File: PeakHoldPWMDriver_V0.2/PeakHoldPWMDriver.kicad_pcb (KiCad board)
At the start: 2 copper layers, 100.1 x 50 mm, 81 parts, among them J1 Screw_Terminal_01x06, J2 Screw_Terminal_01x08, J3 Mounting 3mm, J4 Mounting 3mm, J5 Mounting 3mm, J6 Mounting 3mm, Q1 AO3400, Q10 AO3400, Q11 AO3422, Q12 AO3422, Q13 AO3401A, Q14 BSP78, Q15 AO3401A, Q16 BSP78, Q2 AO3400, Q3 AO3422, Q4 AO3422, Q5 AO3401A, Q6 AO3401A, Q7 BSP78, Q8 BSP78, Q9 AO3400, U1 74LS32, U2 LM2901, U3 74LS74, U4 LTC6992, U5 74LS74, U6 LM78M05_TO220, U7 74LS08, U8 74LS08

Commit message: Routing board V0.2
Work done on new PCB
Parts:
- removed the D6 at (126.6, 101.9)
- removed the D7 at (149.6, 101.9)
- removed J3, J4, J5, J6: Mounting 3mm, MountingHole:MountingHole_3.2mm_M3_DIN965_Pad
- removed the R6 at (130.4, 101.9)
- removed the U7 at (166.0, 104.4)
- added C1: SVPF 1,0M 16, Capacitor_SMD:CP_Elec_10x12.5, F.Cu at (149.9, 101.6)
- added C10: 220nf, Capacitor_SMD:C_0603_1608Metric_Pad1.05x0.95mm_HandSolder, F.Cu at (141.1, 71.4)
- added C2: SVPF 1,0M 16, Capacitor_SMD:CP_Elec_10x12.5, F.Cu at (149.9, 79.8)
- added C3: SVPF 1,0M 16, Capacitor_SMD:CP_Elec_10x12.5, F.Cu at (149.9, 90.7)
- added H1: MountingHole_Pad, MountingHole:MountingHole_2.5mm_Pad, F.Cu at (125.7, 69.8)
- added H2: MountingHole_Pad, MountingHole:MountingHole_2.5mm_Pad, F.Cu at (125.7, 111.8)
- added H3: MountingHole_Pad, MountingHole:MountingHole_2.5mm_Pad, F.Cu at (201.4, 69.8)
- added H4: MountingHole_Pad, MountingHole:MountingHole_2.5mm_Pad, F.Cu at (201.4, 111.8)
- added R8: 8K2, Resistor_SMD:R_0603_1608Metric_Pad1.05x0.95mm_HandSolder, F.Cu at (141.1, 68.3)
- added TP1: PeakTP, TestPoint:TestPoint_Pad_1.0x1.0mm, F.Cu at (207.3, 68.3)
- added TP2: HoldTP, TestPoint:TestPoint_Pad_1.0x1.0mm, F.Cu at (142.0, 73.7)
- added U8: 74LS08, Package_SO:SO-14_5.3x10.2mm_P1.27mm, F.Cu at (161.0, 109.2)
- D1, D4: value LL4148 -> BAV103
- D3: value 40V-1A -> 1N4007
- D6: renamed from D8; value SS310 -> 1N4007
- D7: renamed from D9; value SS310 -> 1N4007
- D8: renamed from D10; value SS310 -> 1N4007
- D9: renamed from D11; value SS310 -> 1N4007
- J1: footprint Connector_Phoenix_MSTB:PhoenixContact_MSTBV_2,5_6-GF-5,08_1x06_P5.08mm_Vertical_ThreadedFlange -> Connector_Phoenix_MSTB:PhoenixContact_MSTBA_2,5_6-G-5,08_1x06_P5.08mm_Horizontal
- J2: footprint Connector_Phoenix_MSTB:PhoenixContact_MSTBV_2,5_8-GF-5,08_1x08_P5.08mm_Vertical_ThreadedFlange -> Connector_Phoenix_MSTB:PhoenixContact_MSTBA_2,5_8-G-5,08_1x08_P5.08mm_Horizontal
- Q11, Q12, Q3, Q4: value AO3422 -> 2N7002
- Q13, Q15, Q5, Q6: value AO3401A -> TSM2309
- U6: footprint Package_TO_SOT_THT:TO-220-3_Vertical -> Package_TO_SOT_SMD:SOT-223-3_TabPin2
- moved D4 43.2 mm to (191.8, 73.4)
- moved R6 40.6 mm to (196.2, 73.2)
- moved RV2 30.4 mm to (193.8, 69.3)
- moved C5 28.2 mm to (126.0, 105.2), turned to 180 degrees
- moved J1 27.2 mm to (115.8, 76.7), turned to 270 degrees
- moved C8 23.8 mm to (131.6, 105.2), turned to 0 degrees
- moved U3 22.5 mm to (171.9, 109.2), turned to 0 degrees
- moved C9 22.4 mm to (136.3, 105.2), turned to 0 degrees
- moved C7 21.0 mm to (136.3, 107.7), turned to 0 degrees
- moved R1 18.2 mm to (114.9, 112.8), turned to 45 degrees
- moved U5 18.1 mm to (171.9, 72.9), turned to 0 degrees
- moved F2 16.9 mm to (121.7, 99.6)
- moved RV1 16.7 mm to (117.9, 69.6)
- moved D3 12.5 mm to (127.0, 99.6), turned to 90 degrees
- moved R18 12.5 mm to (174.5, 101.9), turned to 0 degrees
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- renumbered C1 to C5, C2 to C6, C3 to C7, C4 to C8, C5 to C9, R7 to R6, R8 to R7, U8 to U7
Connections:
- C5 pad 2: Net-(C1-Pad2) -> Net-(C5-Pad2)
- C7 pad 2: Net-(C1-Pad2) -> Net-(C5-Pad2)
- D3 pad 1: Net-(D3-Pad1) -> Net-(C5-Pad2)
- D3 pad 2: Net-(C1-Pad2) -> Net-(D3-Pad2)
- F2 pad 2: Net-(D3-Pad1) -> Net-(D3-Pad2)
- J1 pad 1: VBAT_IN -> INJ4
- J1 pad 2: PWR_GND -> INJ3
- J1 pad 3: INJ1 -> INJ2
- J1 pad 4: INJ2 -> INJ1
- J1 pad 5: INJ3 -> PWR_GND
- J1 pad 6: INJ4 -> VBAT_IN
- U2 pad 10: VREF -> Net-(Q16-Pad3)
- U2 pad 11: Net-(Q8-Pad3) -> VREF
- U2 pad 13: Net-(R19-Pad2) -> Net-(R31-Pad2)
- U2 pad 14: Net-(R31-Pad2) -> Net-(R19-Pad2)
- U2 pad 4: VREF -> Net-(Q7-Pad3)
- U2 pad 5: Net-(Q7-Pad3) -> VREF
- U2 pad 6: VREF -> Net-(Q14-Pad3)
- U2 pad 7: Net-(Q14-Pad3) -> VREF
- U2 pad 8: VREF -> Net-(Q8-Pad3)
- U2 pad 9: Net-(Q16-Pad3) -> VREF
- U6 pad 1: Net-(C1-Pad2) -> Net-(C5-Pad2)
- U7 pad 10: inv_INJ4 -> inv_INJ3
- U7 pad 11: Net-(U1-Pad13) -> Net-(U1-Pad10)
- U7 pad 12: Net-(U5-Pad8) -> Net-(U5-Pad6)
- U7 pad 13: inv_INJ4 -> inv_INJ3
- U7 pad 2: inv_INJ3 -> inv_INJ1
- U7 pad 3: Net-(U1-Pad9) -> Net-(U1-Pad1)
- U7 pad 4: Net-(U5-Pad6) -> Net-(U5-Pad8)
- U7 pad 5: inv_INJ3 -> inv_INJ4
- U7 pad 6: Net-(U1-Pad10) -> Net-(U1-Pad13)
- U7 pad 8: Net-(U1-Pad12) -> Net-(U1-Pad9)
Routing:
- net PWR_GND: track 509.7 -> 63.6 mm, vias 56 -> 0
- net 5V: track 253.7 -> 0.00 mm, vias 18 -> 0
- net PWM: track 84.8 -> 0.00 mm, vias 6 -> 0
- net inv_INJ2: track 70.8 -> 0.00 mm, vias 2 -> 0
- net Net-(Q5-Pad1): track 64.8 -> 0.00 mm, vias 3 -> 0
- net inv_INJ3: track 64.8 -> 0.00 mm, vias 3 -> 0
- net inv_INJ4: track 63.4 -> 0.00 mm, vias 3 -> 0
- net Net-(Q13-Pad1): track 56.4 -> 0.00 mm, vias 2 -> 0
- net Net-(Q15-Pad1): track 47.6 -> 0.00 mm, vias 2 -> 0
- net inv_INJ1: track 46.0 -> 0.00 mm, vias 3 -> 0
- net Net-(Q7-Pad1): track 44.0 -> 0.00 mm, vias 2 -> 0
- net Net-(Q6-Pad1): track 38.6 -> 0.00 mm, vias 2 -> 0
- net Net-(Q16-Pad1): track 36.3 -> 0.00 mm, vias 2 -> 0
- net Net-(C1-Pad2): track 32.2 -> 0.00 mm
- net Net-(U5-Pad8): track 31.6 -> 0.00 mm
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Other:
- board text removed: "13.8V"
- board text removed: "5V"

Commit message: routed V0.2
New board fully routed
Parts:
- D6, D7, D8, D9: value 1N4007 -> SS33
- moved RV1 29.3 mm to (147.2, 70.1), turned to 180 degrees
- moved D1 24.2 mm to (154.2, 70.1)
- moved R2 20.7 mm to (151.4, 70.2), turned to 270 degrees
- moved U1 10.9 mm to (162.3, 91.4)
- moved R3 10.7 mm to (120.1, 69.2), turned to 90 degrees
- moved U2 10.3 mm to (173.6, 91.4)
- moved R28 8.07 mm to (184.3, 94.7), turned to 180 degrees
- moved R17 7.68 mm to (184.3, 88.1), turned to 180 degrees
- moved R24 7.11 mm to (130.9, 77.7)
- moved R16 6.62 mm to (191.0, 99.9)
- moved U4 5.78 mm to (131.1, 70.9), turned to 90 degrees
- moved R18 5.59 mm to (168.9, 101.9), turned to 180 degrees
- moved R29 5.45 mm to (174.9, 101.9), turned to 0 degrees
- moved R11 5.33 mm to (131.0, 82.5)
- moved R22 3.56 mm to (131.0, 87.4)
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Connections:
- U2 pad 10: Net-(Q16-Pad3) -> Net-(Q8-Pad3)
- U2 pad 13: Net-(R31-Pad2) -> Net-(R19-Pad2)
- U2 pad 14: Net-(R19-Pad2) -> Net-(R31-Pad2)
- U2 pad 8: Net-(Q8-Pad3) -> Net-(Q16-Pad3)
- U7 pad 2: inv_INJ1 -> inv_INJ4
- U7 pad 3: Net-(U1-Pad1) -> Net-(U1-Pad12)
- U8 pad 10: inv_INJ4 -> inv_INJ1
- U8 pad 8: Net-(U1-Pad12) -> Net-(U1-Pad1)
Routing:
- net PWR_GND: track 63.6 -> 458.5 mm, vias 0 -> 62
- net 5V: track 0.00 -> 310.1 mm, vias 0 -> 21
- net PWM: track 0.00 -> 115.9 mm, vias 0 -> 7
- net inv_INJ2: track 0.00 -> 78.9 mm, vias 0 -> 2
- net inv_INJ1: track 0.00 -> 72.8 mm, vias 0 -> 2
- net inv_INJ3: track 0.00 -> 69.4 mm, vias 0 -> 2
- net inv_INJ4: track 0.00 -> 68.7 mm
- net Net-(Q5-Pad1): track 0.00 -> 65.2 mm, vias 0 -> 2
- net Net-(Q13-Pad1): track 0.00 -> 59.8 mm, vias 0 -> 2
- net Net-(Q15-Pad1): track 0.00 -> 58.8 mm, vias 0 -> 2
- net VREF: track 18.6 -> 76.6 mm, vias 0 -> 3
- net Net-(Q16-Pad1): track 0.00 -> 54.5 mm, vias 0 -> 4
- net Net-(Q7-Pad1): track 0.00 -> 52.5 mm, vias 0 -> 4
- net Net-(Q6-Pad1): track 0.00 -> 45.9 mm, vias 0 -> 2
- net Net-(Q14-Pad1): track 0.00 -> 42.2 mm
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- added copper zone on F.Cu, net INJ1-OUT
- added copper zone on F.Cu, net INJ2-OUT
- added copper zone on F.Cu, net INJ3-OUT
- added copper zone on F.Cu, net INJ4-OUT
- added copper zone on B.Cu, net inv_INJ1

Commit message: Cleanup of board
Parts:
- C1, C2, C3: value SVPF 1,0M 16 -> 1mF
- D2: value SS310 -> BAV103
- D6, D7, D8, D9: value SS33 -> SS36
- R14, R15, R2, R26, R27, R6: value 470 -> 470R
- R5: value 180 -> 180R
- R8: value 8K2 -> 10k
- U6: value LM78M05_TO220 -> LM78M05
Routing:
- net PWR_GND: track 458.5 -> 446.9 mm, vias 62 -> 99
- net Net-(Q14-Pad3): track 36.4 -> 39.6 mm
- net Net-(Q14-Pad1): track 42.2 -> 44.3 mm
- net Net-(Q8-Pad1): track 42.2 -> 43.3 mm
- net VBAT: vias 13 -> 14
- net INJ1-OUT: vias 0 -> 5
- net INJ4-OUT: vias 0 -> 3
- net INJ3-OUT: vias 0 -> 4
- net INJ2-OUT: vias 0 -> 3
- added copper zone on B.Cu, net INJ1-OUT
- added copper zone on B.Cu, net INJ2-OUT
- added copper zone on B.Cu, net INJ3-OUT
- added copper zone on B.Cu, net INJ4-OUT
- removed copper zone on B.Cu, net inv_INJ1
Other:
- board text added: "PWM Peak&Hold Injector driver"
- board text added: "by Tjeerd V0.2"
- board text removed: "PWM Peak&Hold Injector driver 4Cyl. by Tjeerd"

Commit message: further clean-up
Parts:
- moved R13 0.28 mm to (141.7, 83.3)
- moved R25 0.28 mm to (141.7, 78.5)
- moved RV1 0.20 mm to (147.3, 70.3)
- moved C10 0.14 mm to (141.0, 71.4)
- moved C6 0.14 mm to (137.7, 74.7)
- moved R10 0.14 mm to (130.8, 92.5)
- moved R11 0.14 mm to (130.8, 82.5)
- moved R22 0.14 mm to (130.8, 87.4)
- moved R8 0.14 mm to (141.0, 68.3)
- moved D5 0.11 mm to (121.2, 94.2)
- moved R12 0.11 mm to (141.7, 93.0)
- moved R14 0.11 mm to (179.1, 113.8)
- moved R19 0.11 mm to (169.2, 80.5)
- moved R2 0.11 mm to (151.4, 70.4)
- moved R24 0.11 mm to (130.8, 77.7)
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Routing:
- net VBAT: vias 14 -> 13

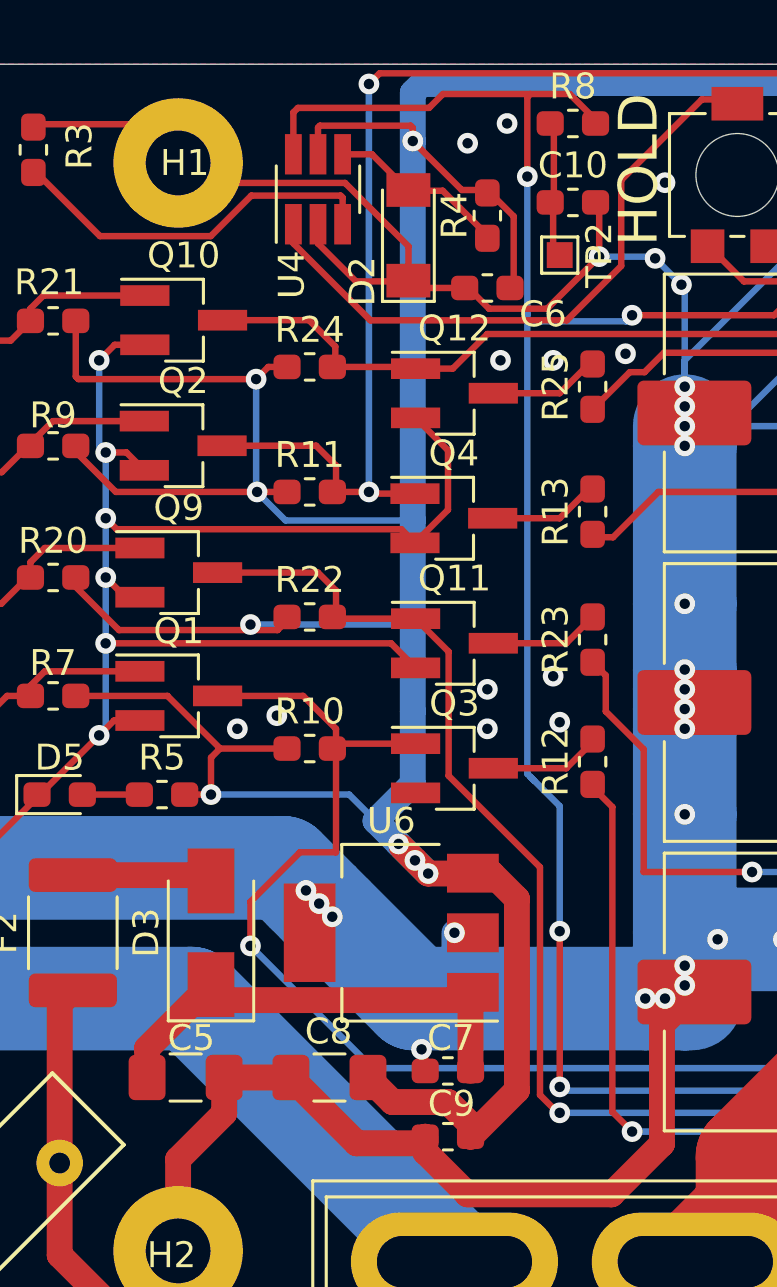
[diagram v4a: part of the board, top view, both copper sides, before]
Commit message: renumber all parts
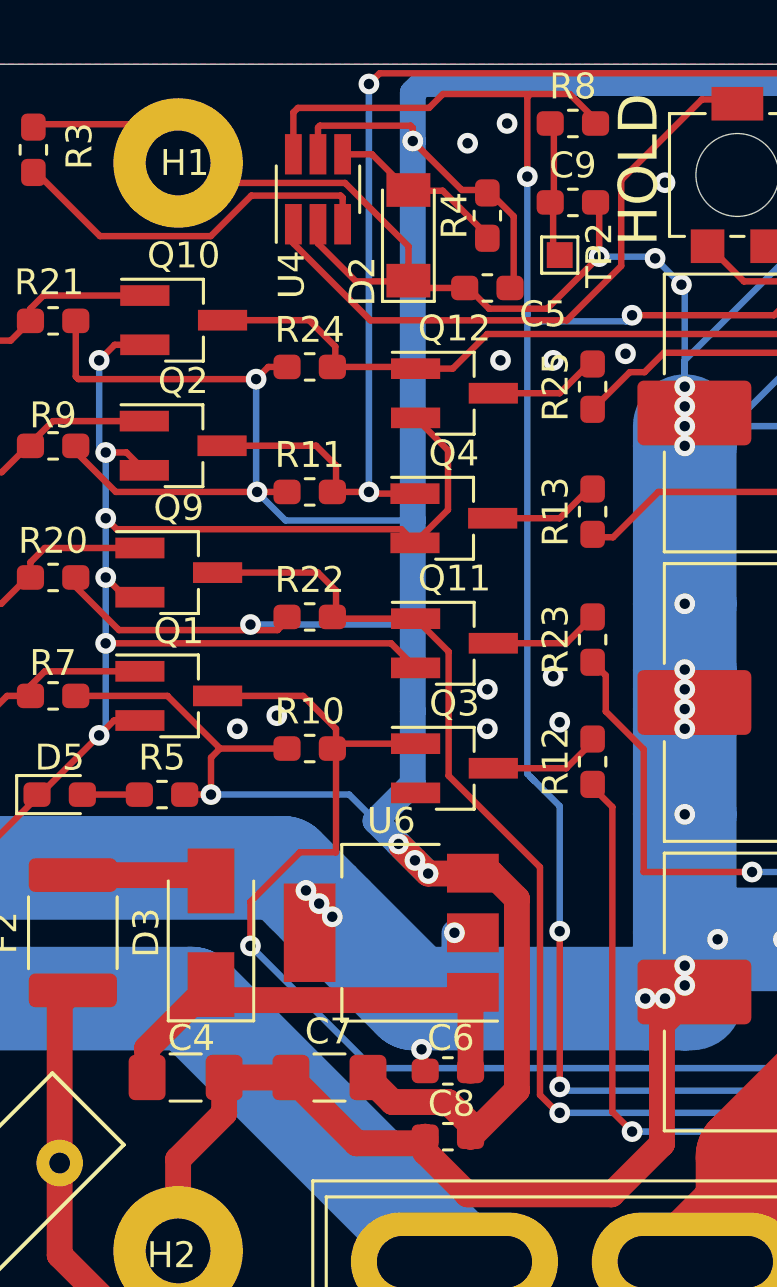
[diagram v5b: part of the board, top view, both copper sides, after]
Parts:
- renumbered C5 to C4, C6 to C5, C7 to C6, C8 to C7, C9 to C8, C10 to C9
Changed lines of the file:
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@@
   (net 62 "Net-(U5-Pad9)")
   (net 63 "Net-(U5-Pad5)")
-  (net 64 "Net-(C5-Pad2)")
-  (net 65 "Net-(C10-Pad1)")
-  (net 66 "Net-(D3-Pad2)")
-  (net 67 "Net-(D7-Pad2)")
+  (net 64 "Net-(D3-Pad2)")
+  (net 65 "Net-(D7-Pad2)")
+  (net 66 "Net-(C4-Pad2)")
+  (net 67 "Net-(C9-Pad1)")
   (net_class Default "This is the default net class."
     (clearance 0.2)
@@
     (add_net INJ4)
     (add_net INJ4-OUT)
-    (add_net "Net-(C10-Pad1)")
-    (add_net "Net-(C5-Pad2)")
+    (add_net "Net-(C4-Pad2)")
+    (add_net "Net-(C9-Pad1)")
     (add_net "Net-(D1-Pad2)")
     (add_net "Net-(D2-Pad2)")
@@
     )
     (pad 2 smd rect (at 2 0 90) (size 2.5 1.8) (layers F.Cu F.Paste F.Mask)
-      (net 66 "Net-(D3-Pad2)"))
+      (net 64 "Net-(D3-Pad2)"))
     (pad 1 smd rect (at -2 0 90) (size 2.5 1.8) (layers F.Cu F.Paste F.Mask)
-      (net 64 "Net-(C5-Pad2)"))
+      (net 66 "Net-(C4-Pad2)"))
     (model ${KISYS3DMOD}/Diode_SMD.3dshapes/D_SMA.wrl
       (at (xyz 0 0 0))
@@
     )
     (pad 2 smd rect (at 2 0 180) (size 2.5 1.8) (layers F.Cu F.Paste F.Mask)
-      (net 67 "Net-(D7-Pad2)"))
+      (net 65 "Net-(D7-Pad2)"))
     (pad 1 smd rect (at -2 0 180) (size 2.5 1.8) (layers F.Cu F.Paste F.Mask)
       (net 2 VBAT))
@@
     )
     (pad 1 smd rect (at -3.15 -2.3 180) (size 2 1.5) (layers F.Cu F.Paste F.Mask)
-      (net 64 "Net-(C5-Pad2)"))
+      (net 66 "Net-(C4-Pad2)"))
     (pad 3 smd rect (at -3.15 2.3 180) (size 2 1.5) (layers F.Cu F.Paste F.Mask)
       (net 1 5V))
@@
     )
     (pad 1 smd rect (at 0 0 90) (size 1 1) (layers F.Cu F.Mask)
-      (net 65 "Net-(C10-Pad1)"))
+      (net 67 "Net-(C9-Pad1)"))
   )
   (module TestPoint:TestPoint_Pad_1.0x1.0mm (layer F.Cu)
@@
       (net 14 PWM))
     (pad 1 smd roundrect (at -0.875 0) (size 1.05 0.95) (layers F.Cu F.Paste F.Mask) (roundrect_rratio 0.25)
-      (net 65 "Net-(C10-Pad1)"))
+      (net 67 "Net-(C9-Pad1)"))
     (model ${KISYS3DMOD}/Resistor_SMD.3dshapes/R_0603_1608Metric.wrl
       (at (xyz 0 0 0))
@@
     (tags "capacitor handsolder")
     (attr smd)
-    (fp_text reference C10 (at 0 -1.43) (layer F.SilkS)
+    (fp_text reference C9 (at 0 -1.43) (layer F.SilkS)
       (effects (font (size 1 1) (thickness 0.15)))
     )
@@
       (net 17 PWR_GND))
     (pad 1 smd roundrect (at -0.875 0) (size 1.05 0.95) (layers F.Cu F.Paste F.Mask) (roundrect_rratio 0.25)
-      (net 65 "Net-(C10-Pad1)"))
+      (net 67 "Net-(C9-Pad1)"))
     (model ${KISYS3DMOD}/Capacitor_SMD.3dshapes/C_0603_1608Metric.wrl
       (at (xyz 0 0 0))
@@
     )
     (pad 3 smd rect (at 1.5 0 180) (size 1.9 0.8) (layers F.Cu F.Paste F.Mask)
-      (net 67 "Net-(D7-Pad2)"))
+      (net 65 "Net-(D7-Pad2)"))
     (pad 2 smd rect (at -1.5 0.95 180) (size 1.9 0.8) (layers F.Cu F.Paste F.Mask)
       (net 5 INJ3-OUT))
@@
     )
     (pad 2 smd roundrect (at 2.225 0 90) (size 1.3 3.4) (layers F.Cu F.Paste F.Mask) (roundrect_rratio 0.192308)
-      (net 66 "Net-(D3-Pad2)"))
+      (net 64 "Net-(D3-Pad2)"))
     (pad 1 smd roundrect (at -2.225 0 90) (size 1.3 3.4) (layers F.Cu F.Paste F.Mask) (roundrect_rratio 0.192308)
       (net 2 VBAT))
@@
     (tags "capacitor handsolder")
     (attr smd)
-    (fp_text reference C8 (at -0.0365 -1.778) (layer F.SilkS)
+    (fp_text reference C7 (at -0.0365 -1.778) (layer F.SilkS)
       (effects (font (size 1 1) (thickness 0.15)))
     )
@@
     (tags "capacitor handsolder")
     (attr smd)
-    (fp_text reference C5 (at -0.2175 1.524) (layer F.SilkS)
+    (fp_text reference C4 (at -0.2175 1.524) (layer F.SilkS)
       (effects (font (size 1 1) (thickness 0.15)))
     )
@@
     )
     (pad 2 smd roundrect (at 1.4875 0 180) (size 1.425 1.75) (layers F.Cu F.Paste F.Mask) (roundrect_rratio 0.175439)
-      (net 64 "Net-(C5-Pad2)"))
+      (net 66 "Net-(C4-Pad2)"))
     (pad 1 smd roundrect (at -1.4875 0 180) (size 1.425 1.75) (layers F.Cu F.Paste F.Mask) (roundrect_rratio 0.175439)
       (net 17 PWR_GND))
@@
     (tags "capacitor handsolder")
     (attr smd)
-    (fp_text reference C6 (at -2.145 -1.016) (layer F.SilkS)
+    (fp_text reference C5 (at -2.145 -1.016) (layer F.SilkS)
       (effects (font (size 1 1) (thickness 0.15)))
     )
@@
     (tags "capacitor handsolder")
     (attr smd)
-    (fp_text reference C9 (at 0.141 -1.27) (layer F.SilkS)
+    (fp_text reference C8 (at 0.141 -1.27) (layer F.SilkS)
       (effects (font (size 1 1) (thickness 0.15)))
     )
@@
     (tags "capacitor handsolder")
     (attr smd)
-    (fp_text reference C7 (at 0.113 -1.27) (layer F.SilkS)
+    (fp_text reference C6 (at 0.113 -1.27) (layer F.SilkS)
       (effects (font (size 1 1) (thickness 0.15)))
     )
@@
     )
     (pad 2 smd roundrect (at 0.875 0) (size 1.05 0.95) (layers F.Cu F.Paste F.Mask) (roundrect_rratio 0.25)
-      (net 64 "Net-(C5-Pad2)"))
+      (net 66 "Net-(C4-Pad2)"))
     (pad 1 smd roundrect (at -0.875 0) (size 1.05 0.95) (layers F.Cu F.Paste F.Mask) (roundrect_rratio 0.25)
       (net 17 PWR_GND))
@@
   (segment (start 166.878 112.014) (end 168.335 112.014) (width 0.25) (layer F.Cu) (net 60) (status 20))
   (segment (start 166.624 111.76) (end 166.878 112.014) (width 0.25) (layer F.Cu) (net 60))
-  (segment (start 124.533 104.035) (end 127 101.568) (width 1) (layer F.Cu) (net 64) (status 20))
-  (segment (start 124.533 105.156) (end 124.533 104.035) (width 1) (layer F.Cu) (net 64) (status 10))
-  (segment (start 136.809999 102.168001) (end 137.11 101.868) (width 1) (layer F.Cu) (net 64) (status 30))
-  (segment (start 127.600001 102.168001) (end 136.809999 102.168001) (width 1) (layer F.Cu) (net 64) (status 30))
-  (segment (start 127 101.568) (end 127.600001 102.168001) (width 1) (layer F.Cu) (net 64) (status 30))
-  (segment (start 137.019 101.959) (end 137.11 101.868) (width 1) (layer F.Cu) (net 64) (status 30))
-  (segment (start 137.019 104.902) (end 137.019 101.959) (width 1) (layer F.Cu) (net 64) (status 30))
-  (segment (start 140.208 71.402) (end 140.236 71.374) (width 0.25) (layer F.Cu) (net 65) (status 30))
-  (segment (start 140.208 73.406) (end 140.208 71.402) (width 0.25) (layer F.Cu) (net 65) (status 30))
-  (segment (start 140.236 71.374) (end 140.236 68.326) (width 0.25) (layer F.Cu) (net 65) (status 30))
-  (segment (start 126.775 97.343) (end 127 97.568) (width 1) (layer F.Cu) (net 66) (status 30))
-  (segment (start 121.666 97.343) (end 126.775 97.343) (width 1) (layer F.Cu) (net 66) (status 30))
-  (segment (start 182.904 77.462) (end 181.896 76.454) (width 1) (layer F.Cu) (net 67) (status 20))
-  (segment (start 182.904 80.518) (end 182.904 77.462) (width 1) (layer F.Cu) (net 67) (status 10))
+  (segment (start 124.533 104.035) (end 127 101.568) (width 1) (layer F.Cu) (net 66) (status 20))
+  (segment (start 124.533 105.156) (end 124.533 104.035) (width 1) (layer F.Cu) (net 66) (status 10))
+  (segment (start 136.809999 102.168001) (end 137.11 101.868) (width 1) (layer F.Cu) (net 66) (status 30))
+  (segment (start 127.600001 102.168001) (end 136.809999 102.168001) (width 1) (layer F.Cu) (net 66) (status 30))
+  (segment (start 127 101.568) (end 127.600001 102.168001) (width 1) (layer F.Cu) (net 66) (status 30))
+  (segment (start 137.019 101.959) (end 137.11 101.868) (width 1) (layer F.Cu) (net 66) (status 30))
+  (segment (start 137.019 104.902) (end 137.019 101.959) (width 1) (layer F.Cu) (net 66) (status 30))
+  (segment (start 140.208 71.402) (end 140.236 71.374) (width 0.25) (layer F.Cu) (net 67) (status 30))
+  (segment (start 140.208 73.406) (end 140.208 71.402) (width 0.25) (layer F.Cu) (net 67) (status 30))
+  (segment (start 140.236 71.374) (end 140.236 68.326) (width 0.25) (layer F.Cu) (net 67) (status 30))
+  (segment (start 126.775 97.343) (end 127 97.568) (width 1) (layer F.Cu) (net 64) (status 30))
+  (segment (start 121.666 97.343) (end 126.775 97.343) (width 1) (layer F.Cu) (net 64) (status 30))
+  (segment (start 182.904 77.462) (end 181.896 76.454) (width 1) (layer F.Cu) (net 65) (status 20))
+  (segment (start 182.904 80.518) (end 182.904 77.462) (width 1) (layer F.Cu) (net 65) (status 10))
   (zone (net 17) (net_name PWR_GND) (layer B.Cu) (hatch edge 0.508)
     (connect_pads (clearance 0.254))
